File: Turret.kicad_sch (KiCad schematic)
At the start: 26 parts, among them J1 172298-1108, J2 501645-1620

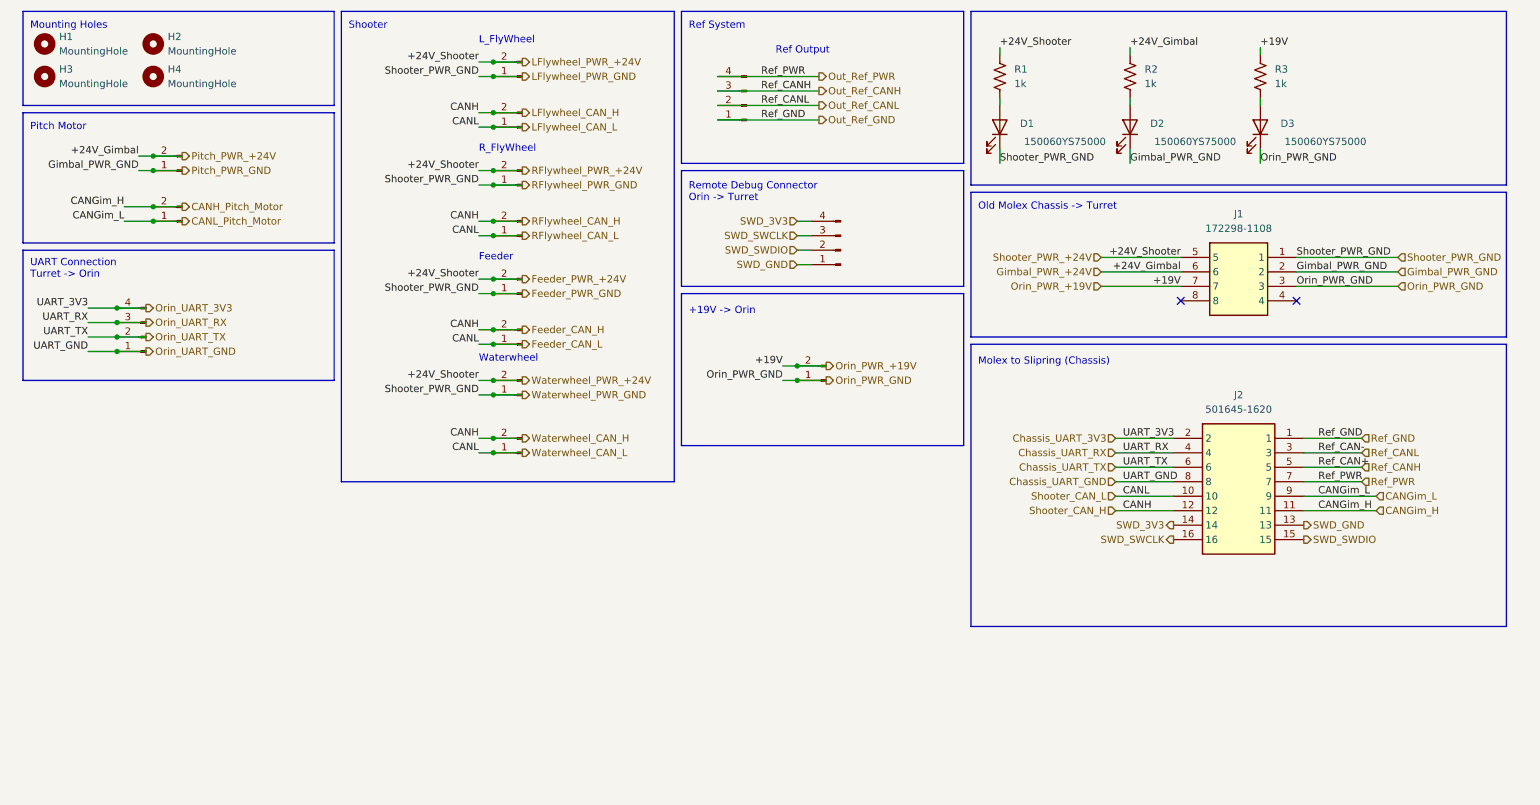
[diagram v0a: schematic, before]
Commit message: Cleaned up hiearchical labels and local labels
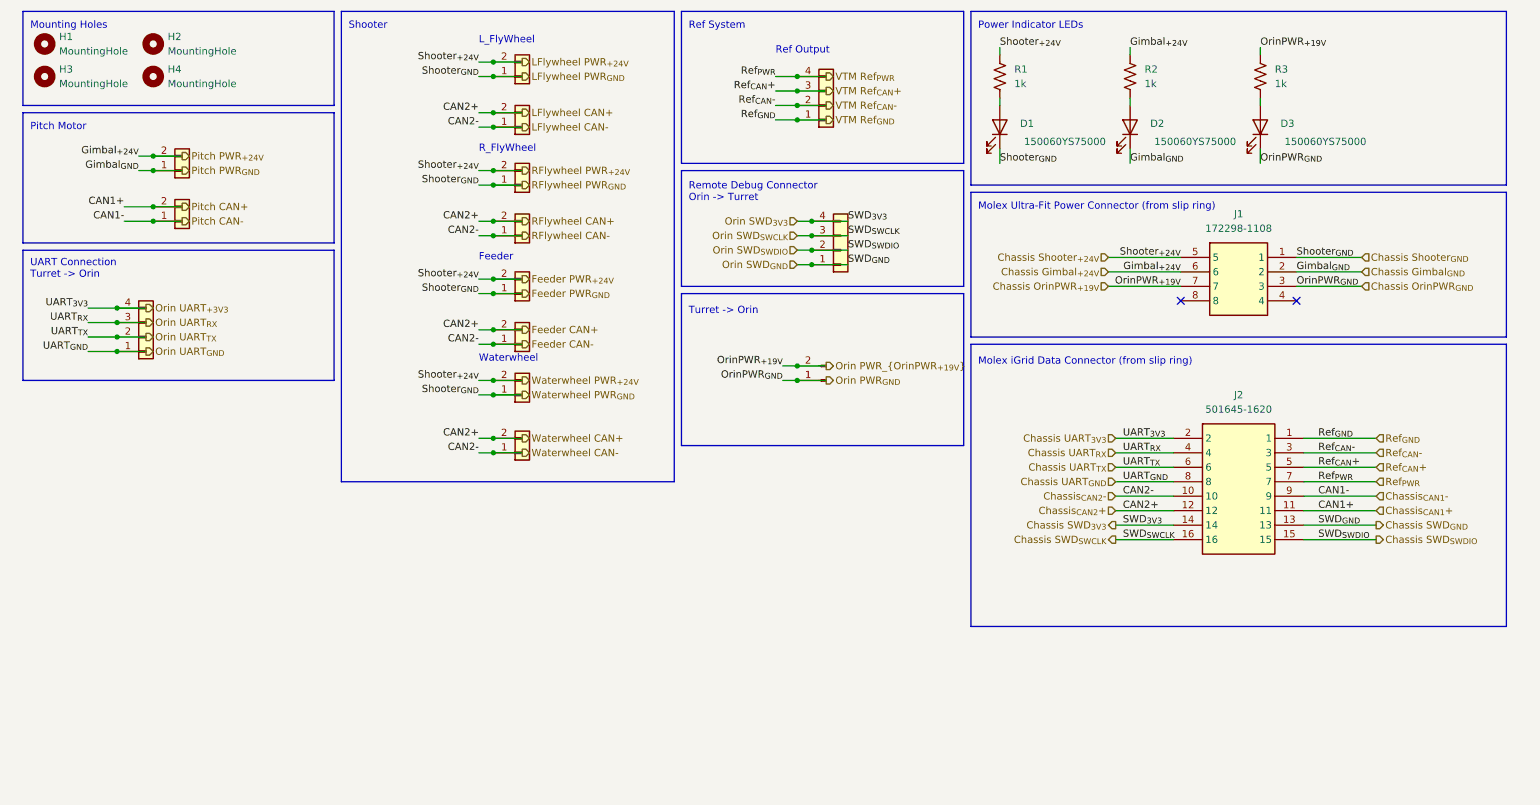
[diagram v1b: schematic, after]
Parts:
- +24V_Feeder1, +24V_Gimbal1, +24V_L_Flywheel1, +24V_R_Flywheel1, +24V_Waterwheel1, CAN_Feeder1, CAN_Gimbal1, CAN_L_Flywheel1, CAN_R_Flywheel1, CAN_Waterwheel1: symbol Connector:Conn_01x02_Pin -> Connector_Generic:Conn_01x02
- Debug_Orin->Turret1, Ref_Out1, UART_Turret->Orin1: symbol Connector:Conn_01x04_Pin -> Connector_Generic:Conn_01x04
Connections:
- net CANGim_H renamed Chassis_{CAN1}+
- net CANGim_L renamed Chassis_{CAN1}-
- net Chassis_UART_3V3 renamed Chassis UART_{3V3}
- net Chassis_UART_GND renamed Chassis UART_{GND}
- net Chassis_UART_RX renamed Chassis UART_{RX}
- net Chassis_UART_TX renamed Chassis UART_{TX}
- net Feeder_CAN_H renamed Chassis_{CAN2}+
- net Feeder_CAN_L renamed Chassis_{CAN2}-
- net Feeder_PWR_+24V renamed Chassis Shooter_{+24V}
- net Feeder_PWR_GND renamed Chassis Shooter_{GND}
- net Gimbal_PWR_+24V renamed Chassis Gimbal_{+24V}
- net Gimbal_PWR_GND renamed Chassis Gimbal_{GND}
- net Orin_PWR_+19V renamed Chassis OrinPWR_{+19V}
- net Orin_PWR_GND renamed Chassis OrinPWR_{GND}
- net Out_Ref_CANH renamed Ref_{CAN}+
- net Out_Ref_CANL renamed Ref_{CAN}-
- net Out_Ref_GND renamed Ref_{GND}
- net Out_Ref_PWR renamed Ref_{PWR}
- net SWD_3V3 renamed Chassis SWD_{3V3}
- net SWD_GND renamed Chassis SWD_{GND}
- net SWD_SWCLK renamed Chassis SWD_{SWCLK}
- net SWD_SWDIO renamed Chassis SWD_{SWDIO}
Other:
- note added: "Molex Ultra-Fit Power Connector (from slip ring)"
- note added: "Molex iGrid Data Connector (from slip ring)"
- note added: "Power Indicator LEDs"
- note added: "Turret -> Orin"
- note removed: "+19V -> Orin"
- note removed: "Molex to Slipring (Chassis)"
- note removed: "Old Molex Chassis -> Turret"

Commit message: Prepped for work
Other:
- note added: "Todo: Swap UART connection just as was done on chassis board. Should now be a SPI connection MAKE SURE PIN NUMBERS MATCH ACROSS CHASSIS AND TURRET BOARDS"
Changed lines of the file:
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@@
+		)
+	)
+	(text "Todo:\nSwap UART connection just as was done on chassis board.\nShould now be a SPI connection\nMAKE SURE PIN NUMBERS MATCH ACROSS CHASSIS AND TURRET BOARDS"
+		(exclude_from_sim no)
+		(at 57.912 112.014 0)
+		(effects
+			(font
+				(size 1.778 1.778)
+				(color 194 0 0 1)
+			)
+			(justify left)
 		)
 	)

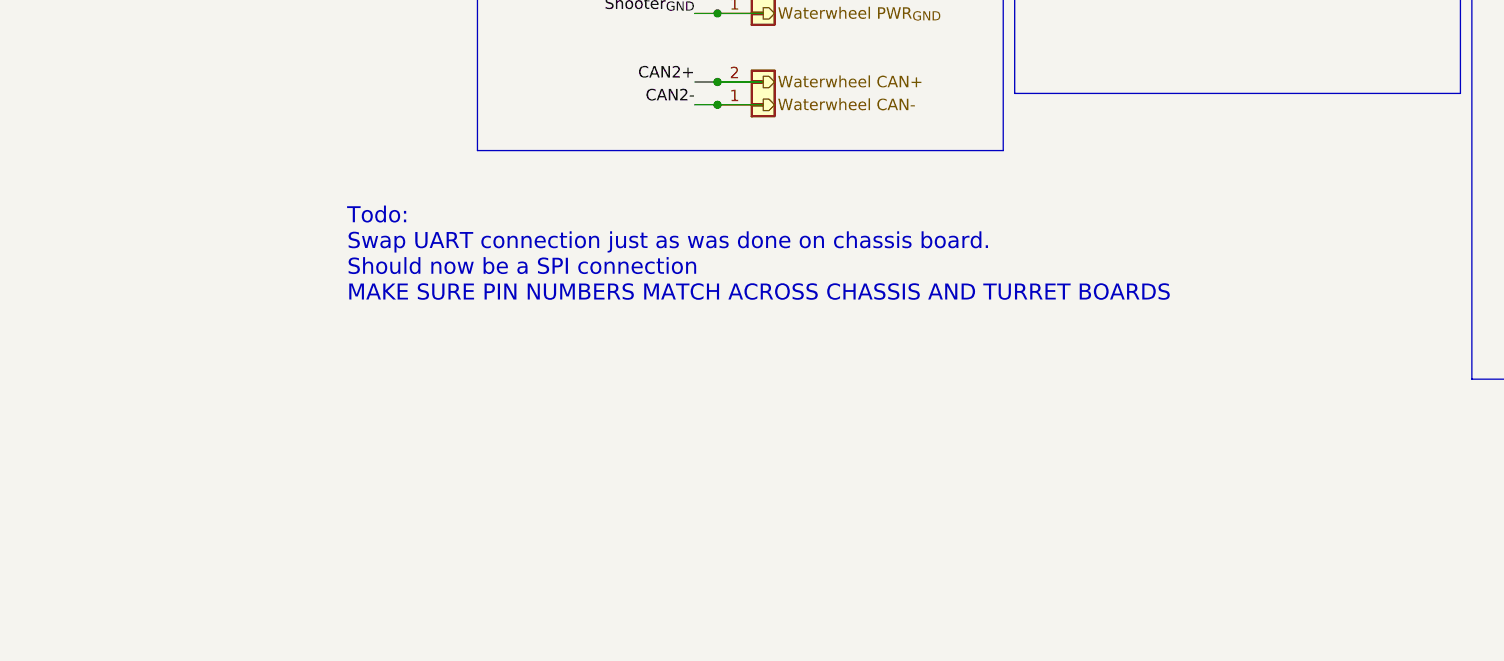
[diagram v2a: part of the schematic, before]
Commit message: Added UV LED connection
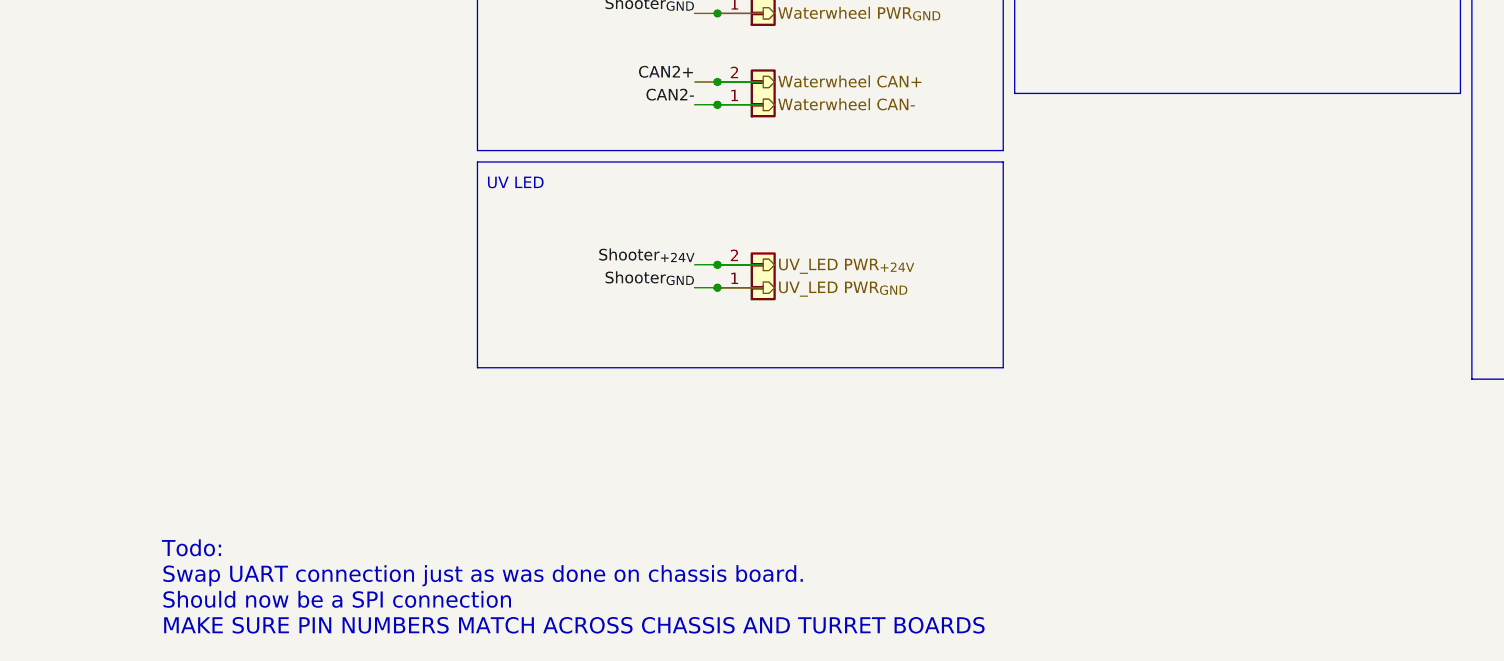
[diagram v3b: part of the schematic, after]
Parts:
- added +24V_Waterwheel2: Conn_01x02_Pin, Connector_AMASS:AMASS_XT30U-F_1x02_P5.0mm_Vertical, symbol Connector_Generic:Conn_01x02
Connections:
- net Chassis Shooter_{+24V}: now also +24V_Waterwheel2.2 (Pin_2)
- net Chassis Shooter_{GND}: now also +24V_Waterwheel2.1 (Pin_1)
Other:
- note added: "UV LED"
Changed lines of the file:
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@@
 	(paper "A4")
 	(rectangle
+		(start 72.39 101.6)
+		(end 130.81 124.46)
+		(stroke
+			(width 0)
+			(type default)
+		)
+		(fill
+			(type none)
+		)
+	)
+	(rectangle
 		(start 132.08 17.78)
 		(end 181.61 44.45)
@@
 	(text "Todo:\nSwap UART connection just as was done on chassis board.\nShould now be a SPI connection\nMAKE SURE PIN NUMBERS MATCH ACROSS CHASSIS AND TURRET BOARDS"
 		(exclude_from_sim no)
-		(at 57.912 112.014 0)
+		(at 37.338 149.098 0)
 		(effects
 			(font
@@
 		)
 	)
+	(text "UV LED"
+		(exclude_from_sim no)
+		(at 73.406 104.902 0)
+		(effects
+			(font
+				(size 1.27 1.27)
+			)
+			(justify left bottom)
+		)
+	)
 	(text "Ref Output\n"
 		(exclude_from_sim no)
@@
 	)
 	(junction
+		(at 99.06 113.03)
+		(diameter 0)
+		(color 0 0 0 0)
+	)
+	(junction
 		(at 154.94 59.69)
 		(diameter 0)
@@
 	)
 	(junction
+		(at 99.06 115.57)
+		(diameter 0)
+		(color 0 0 0 0)
+	)
+	(junction
 		(at 99.06 26.67)
 		(diameter 0)
@@
 	(wire
 		(pts
+			(xy 99.06 113.03) (xy 104.14 113.03)
+		)
+		(stroke
+			(width 0)
+			(type default)
+		)
+	)
+	(wire
+		(pts
 			(xy 96.52 45.72) (xy 99.06 45.72)
 		)
@@
 	(wire
 		(pts
+			(xy 96.52 113.03) (xy 99.06 113.03)
+		)
+		(stroke
+			(width 0)
+			(type default)
+		)
+	)
+	(wire
+		(pts
 			(xy 254 92.71) (xy 241.3 92.71)
 		)
@@
 	(wire
 		(pts
+			(xy 96.52 115.57) (xy 99.06 115.57)
+		)
+		(stroke
+			(width 0)
+			(type default)
+		)
+	)
+	(wire
+		(pts
 			(xy 96.52 85.09) (xy 99.06 85.09)
 		)
@@
 	(wire
 		(pts
+			(xy 99.06 115.57) (xy 104.14 115.57)
+		)
+		(stroke
+			(width 0)
+			(type default)
+		)
+	)
+	(wire
+		(pts
 			(xy 210.82 41.91) (xy 210.82 44.45)
 		)
@@
 	)
 	(label "Shooter_{GND}"
+		(at 96.52 115.57 180)
+		(effects
+			(font
+				(size 1.27 1.27)
+			)
+			(justify right bottom)
+		)
+	)
+	(label "Shooter_{GND}"
 		(at 96.52 85.09 180)
 		(effects
@@
 		)
 	)
+	(label "Shooter_{+24V}"
+		(at 96.52 113.03 180)
+		(effects
+			(font
+				(size 1.27 1.27)
+			)
+			(justify right bottom)
+		)
+	)
 	(label "UART_{3V3}"
 		(at 27.94 69.85 180)
@@
 		)
 	)
+	(hierarchical_label "UV_LED PWR_{GND}"
+		(shape output)
+		(at 104.14 115.57 0)
+		(effects
+			(font
+				(size 1.27 1.27)
+			)
+			(justify left)
+		)
+	)
 	(hierarchical_label "VTM Ref_{CAN}+"
 		(shape output)
@@
 		)
 	)
+	(hierarchical_label "UV_LED PWR_{+24V}"
+		(shape output)
+		(at 104.14 113.03 0)
+		(effects
+			(font
+				(size 1.27 1.27)
+			)
+			(justify left)
+		)
+	)
 	(hierarchical_label "Orin UART_{GND}"
 		(shape output)
@@
 					(unit 1)
 				)
+			)
+		)
+	)
+	(symbol
+		(lib_id "Connector_Generic:Conn_01x02")
+		(at 104.14 115.57 0)
+		(mirror x)
+		(unit 1)
+		(exclude_from_sim no)
+		(in_bom yes)
+		(on_board yes)
+		(dnp no)
+		(property "Reference" "+24V_Waterwheel2"
+			(at 102.87 113.03 0)
+			(effects
+				(font
+					(size 1.27 1.27)
+				)
+				(justify right)
+				(hide yes)
+			)
+		)
+		(property "Value" "Conn_01x02_Pin"
+			(at 102.87 115.57 0)
+			(effects
+				(font
+					(size 1.27 1.27)
+				)
+				(justify right)
+				(hide yes)
+			)
+		)
+		(property "Footprint" "Connector_AMASS:AMASS_XT30U-F_1x02_P5.0mm_Vertical"
+			(at 104.14 115.57 0)
+			(effects
+				(font
+					(size 1.27 1.27)
+				)
+				(hide yes)
+			)
+		)
+		(property "Datasheet" "~"
+			(at 104.14 115.57 0)
+			(effects
+				(font
+					(size 1.27 1.27)
+				)
+				(hide yes)
+			)
+		)
+		(property "Description" "Generic connector, single row, 01x02, script generated (kicad-library-utils/schlib/autogen/connector/)"
+			(at 104.14 115.57 0)
+			(effects
+				(font
+					(size 1.27 1.27)
+				)
+				(hide yes)
+			)
+		)
+		(property "Mouser Part Number" "XT30"
+			(at 104.14 115.57 0)
+			(effects
+				(font
+					(size 1.27 1.27)
+				)
+				(hide yes)
+			)
+		)
+		(pin "1"
+		)
+		(pin "2"
+		)
+		(instances
+			(project "Turret"
+				(path "/84905b3c-2997-4e61-b373-c0062fb72371"
+					(reference "+24V_Waterwheel2")
+					(unit 1)
+				)
